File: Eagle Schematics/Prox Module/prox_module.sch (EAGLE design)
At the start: 52 parts, among them IC1 74LS14N, IC2 74LS14N, Q1 16MHZ

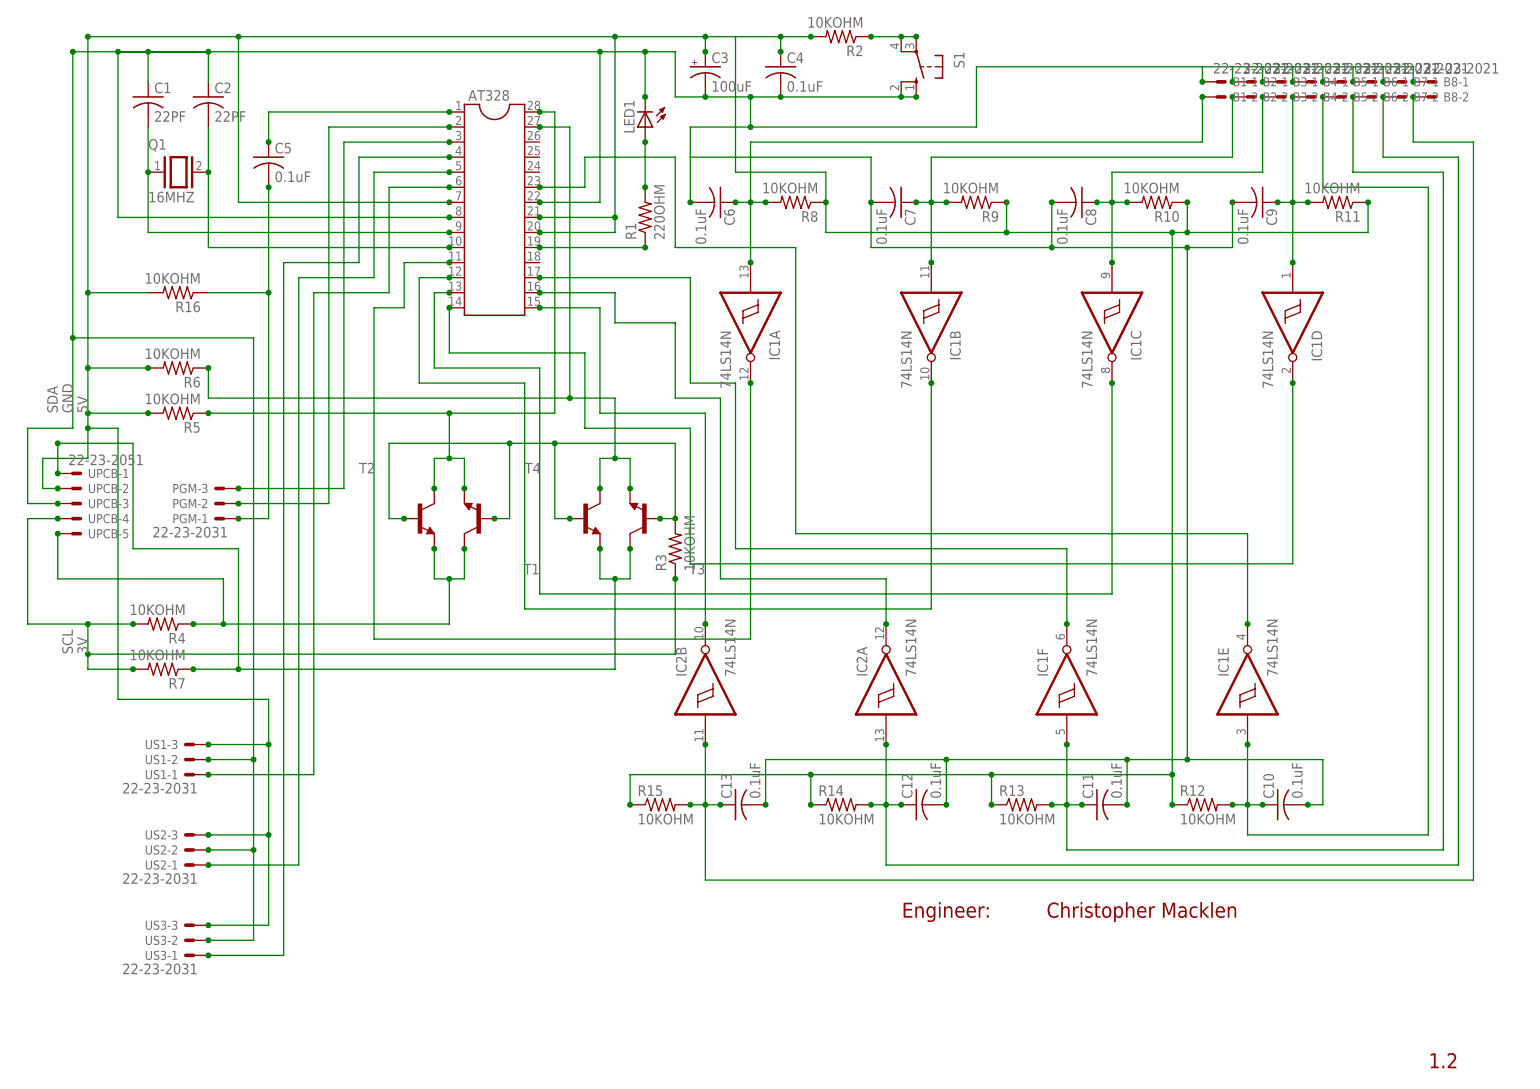
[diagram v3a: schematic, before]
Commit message: Modified prox design, added BOM
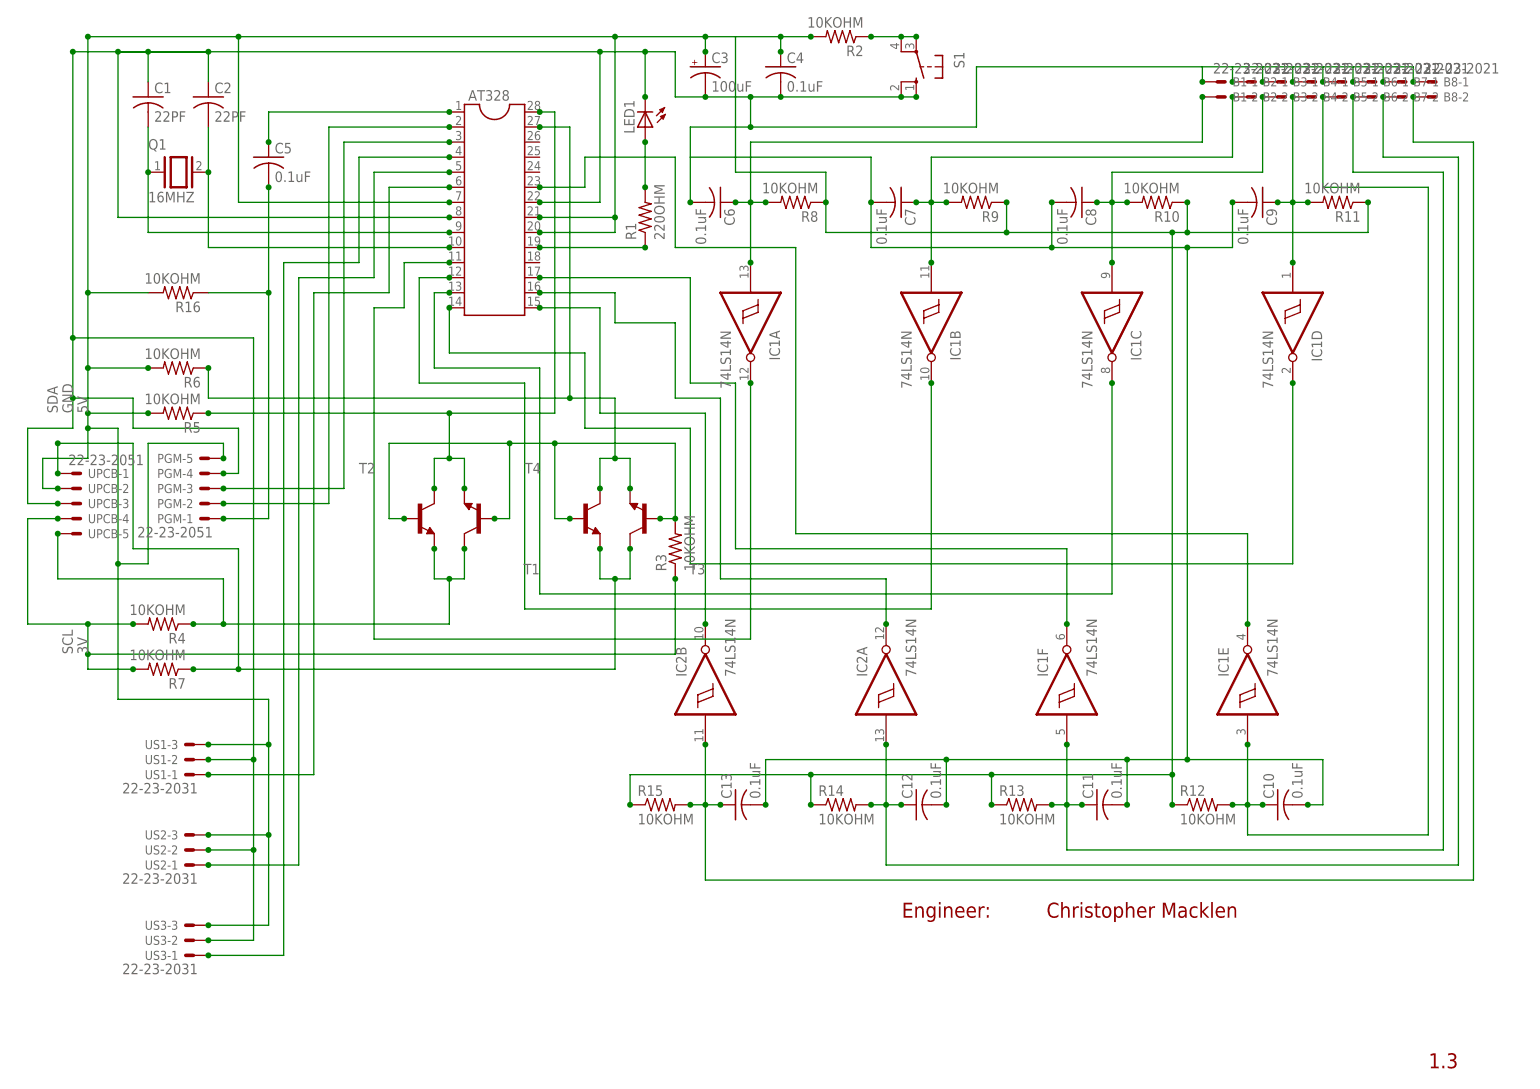
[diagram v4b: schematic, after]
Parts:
- PGM: value 22-23-2031 -> 22-23-2051; device con-molex:22-23-2031 -> con-molex:22-23-2051
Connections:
- net 5V: now also PGM-5.S
- net GND: now also PGM-4.S
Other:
- note added: "1.3"
- note removed: "1.2"
- moved on the sheet: PGM-1, PGM-2, PGM-3
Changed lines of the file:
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@@
 <part name="B7" library="con-molex" deviceset="22-23-2021" device=""/>
 <part name="B8" library="con-molex" deviceset="22-23-2021" device=""/>
-<part name="PGM" library="con-molex" deviceset="22-23-2031" device=""/>
 <part name="US1" library="con-molex" deviceset="22-23-2031" device=""/>
 <part name="US2" library="con-molex" deviceset="22-23-2031" device=""/>
@@
 <part name="R16" library="rcl" deviceset="R-US_" device="0204/7" value="10KOHM"/>
 <part name="C3" library="rcl" deviceset="CPOL-US" device="E2-5" value="100uF"/>
+<part name="PGM" library="con-molex" deviceset="22-23-2051" device=""/>
 </parts>
 <sheets>
@@
 <plain>
 <text x="190.5" y="33.02" size="2.54" layer="94" font="vector" align="center">Christopher Macklen</text>
-<text x="241.3" y="7.62" size="2.54" layer="94" font="vector" align="center">1.2</text>
+<text x="241.3" y="7.62" size="2.54" layer="94" font="vector" align="center">1.3</text>
 <text x="157.48" y="33.02" size="2.54" layer="94" font="vector" align="center">Engineer:</text>
 </plain>
@@
 <instance part="B8" gate="-1" x="238.76" y="172.72"/>
 <instance part="B8" gate="-2" x="238.76" y="170.18"/>
-<instance part="PGM" gate="-1" x="35.56" y="99.06" rot="R180"/>
-<instance part="PGM" gate="-2" x="35.56" y="101.6" rot="R180"/>
-<instance part="PGM" gate="-3" x="35.56" y="104.14" rot="R180"/>
 <instance part="US1" gate="-1" x="30.48" y="55.88" rot="R180"/>
 <instance part="US1" gate="-2" x="30.48" y="58.42" rot="R180"/>
@@
 <instance part="R16" gate="G$1" x="27.94" y="137.16" rot="R180"/>
 <instance part="C3" gate="G$1" x="116.84" y="175.26"/>
+<instance part="PGM" gate="-1" x="33.02" y="99.06" rot="R180"/>
+<instance part="PGM" gate="-2" x="33.02" y="101.6" rot="R180"/>
+<instance part="PGM" gate="-3" x="33.02" y="104.14" rot="R180"/>
+<instance part="PGM" gate="-4" x="33.02" y="106.68" rot="R180"/>
+<instance part="PGM" gate="-5" x="33.02" y="109.22" rot="R180"/>
 </instances>
 <busses>
@@
 <label x="10.16" y="116.84" size="1.778" layer="95" rot="R90"/>
 <pinref part="AT328" gate="G$1" pin="22"/>
-<wire x1="10.16" y1="114.3" x2="10.16" y2="129.54" width="0.1524" layer="91"/>
+<wire x1="10.16" y1="114.3" x2="10.16" y2="119.38" width="0.1524" layer="91"/>
+<wire x1="10.16" y1="119.38" x2="10.16" y2="129.54" width="0.1524" layer="91"/>
 <wire x1="10.16" y1="129.54" x2="10.16" y2="177.8" width="0.1524" layer="91"/>
 <wire x1="88.9" y1="152.4" x2="99.06" y2="152.4" width="0.1524" layer="91"/>
@@
 <pinref part="C3" gate="G$1" pin="-"/>
 <junction x="116.84" y="170.18"/>
+<pinref part="PGM" gate="-4" pin="S"/>
+<wire x1="35.56" y1="106.68" x2="38.1" y2="106.68" width="0.1524" layer="91"/>
+<wire x1="38.1" y1="106.68" x2="38.1" y2="114.3" width="0.1524" layer="91"/>
+<wire x1="38.1" y1="114.3" x2="20.32" y2="114.3" width="0.1524" layer="91"/>
+<wire x1="20.32" y1="114.3" x2="20.32" y2="119.38" width="0.1524" layer="91"/>
+<wire x1="20.32" y1="119.38" x2="10.16" y2="119.38" width="0.1524" layer="91"/>
+<junction x="10.16" y="119.38"/>
+<junction x="35.56" y="106.68"/>
 </segment>
 </net>
@@
 <net name="TX-RX" class="0">
 <segment>
-<wire x1="38.1" y1="101.6" x2="53.34" y2="101.6" width="0.1524" layer="91"/>
+<wire x1="35.56" y1="101.6" x2="53.34" y2="101.6" width="0.1524" layer="91"/>
 <wire x1="53.34" y1="101.6" x2="53.34" y2="165.1" width="0.1524" layer="91"/>
 <pinref part="AT328" gate="G$1" pin="2"/>
@@
 <junction x="73.66" y="165.1"/>
 <pinref part="PGM" gate="-2" pin="S"/>
-<junction x="38.1" y="101.6"/>
+<junction x="35.56" y="101.6"/>
 </segment>
 </net>
 <net name="RX-TX" class="0">
 <segment>
-<wire x1="38.1" y1="104.14" x2="55.88" y2="104.14" width="0.1524" layer="91"/>
+<wire x1="35.56" y1="104.14" x2="55.88" y2="104.14" width="0.1524" layer="91"/>
 <wire x1="55.88" y1="104.14" x2="55.88" y2="162.56" width="0.1524" layer="91"/>
 <pinref part="AT328" gate="G$1" pin="3"/>
@@
 <junction x="73.66" y="162.56"/>
 <pinref part="PGM" gate="-3" pin="S"/>
-<junction x="38.1" y="104.14"/>
+<junction x="35.56" y="104.14"/>
 </segment>
 </net>
@@
 <wire x1="43.18" y1="99.06" x2="43.18" y2="137.16" width="0.1524" layer="91"/>
 <wire x1="43.18" y1="137.16" x2="43.18" y2="154.94" width="0.1524" layer="91"/>
-<wire x1="38.1" y1="99.06" x2="43.18" y2="99.06" width="0.1524" layer="91"/>
-<pinref part="PGM" gate="-1" pin="S"/>
-<junction x="38.1" y="99.06"/>
+<wire x1="35.56" y1="99.06" x2="43.18" y2="99.06" width="0.1524" layer="91"/>
 <pinref part="R16" gate="G$1" pin="1"/>
 <wire x1="33.02" y1="137.16" x2="43.18" y2="137.16" width="0.1524" layer="91"/>
 <junction x="43.18" y="137.16"/>
+<pinref part="PGM" gate="-1" pin="S"/>
+<junction x="35.56" y="99.06"/>
 </segment>
 </net>
@@
 <junction x="22.86" y="124.46"/>
 <wire x1="12.7" y1="114.3" x2="17.78" y2="114.3" width="0.1524" layer="91"/>
-<wire x1="17.78" y1="114.3" x2="17.78" y2="68.58" width="0.1524" layer="91"/>
+<wire x1="17.78" y1="114.3" x2="17.78" y2="91.44" width="0.1524" layer="91"/>
+<wire x1="17.78" y1="91.44" x2="17.78" y2="68.58" width="0.1524" layer="91"/>
 <wire x1="17.78" y1="68.58" x2="43.18" y2="68.58" width="0.1524" layer="91"/>
 <wire x1="43.18" y1="68.58" x2="43.18" y2="60.96" width="0.1524" layer="91"/>
@@
 <pinref part="C3" gate="G$1" pin="+"/>
 <junction x="116.84" y="177.8"/>
-</segment>
-</net>
+<pinref part="PGM" gate="-5" pin="S"/>
+<wire x1="35.56" y1="109.22" x2="35.56" y2="111.76" width="0.1524" layer="91"/>
+<wire x1="35.56" y1="111.76" x2="22.86" y2="111.76" width="0.1524" layer="91"/>
+<wire x1="22.86" y1="111.76" x2="22.86" y2="91.44" width="0.1524" layer="91"/>
+<wire x1="22.86" y1="91.44" x2="17.78" y2="91.44" width="0.1524" layer="91"/>
+<junction x="17.78" y="91.44"/>
+<junction x="35.56" y="109.22"/>
+</segment>
+</net>

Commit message: Made final V1.4 revisions
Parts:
- added C14: 100uF, rcl:CPOL-USE2-5
- added C15: 0.1uF, rcl:C-US025-024X044
- ATMEGA: value (none) -> 328
- T1, T2, T3, T4: value (none) -> BJT
- renumbered AT328 to ATMEGA
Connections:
- net 3V: now also C14.+, C15.1
- net 5V: now also IC1P.VCC, IC2P.VCC
- net GND: now also C14.-, C15.2, IC1P.GND, IC2P.GND
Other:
- note added: "1.4"
- note removed: "1.3"
- moved on the sheet: R4, R7

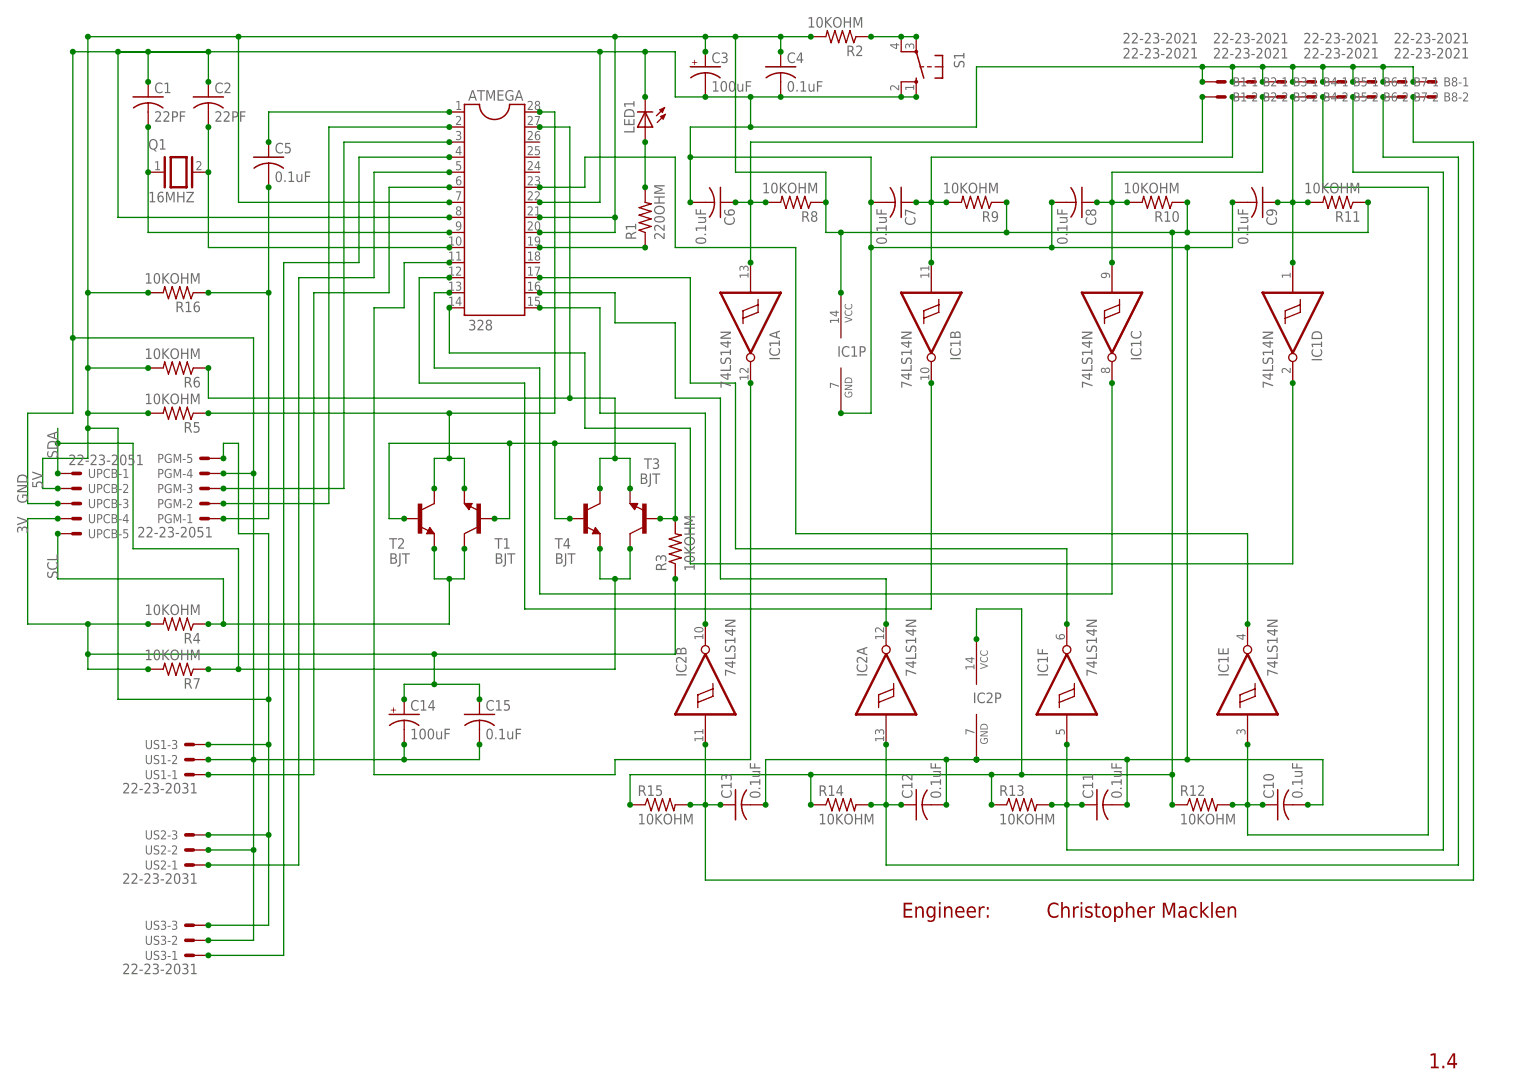
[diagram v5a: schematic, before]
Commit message: Modified all schematics
Added a self debugging system.
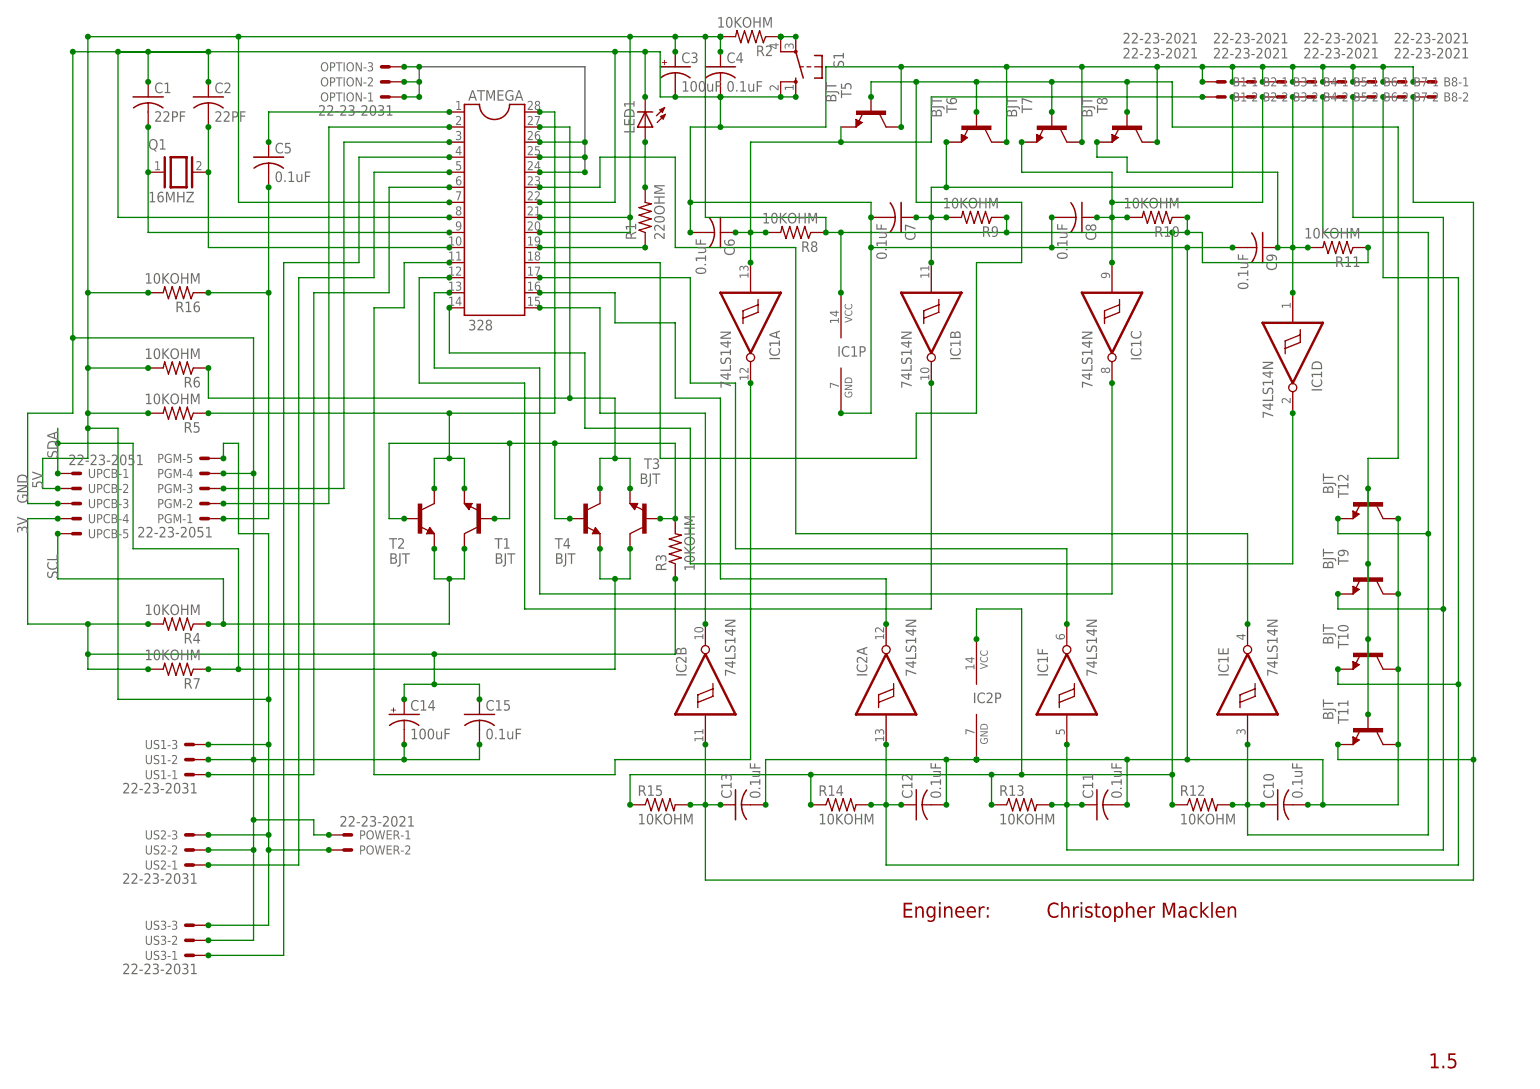
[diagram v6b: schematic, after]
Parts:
- added OPTION: 22-23-2031, con-molex:22-23-2031
- added POWER: 22-23-2021, con-molex:22-23-2021
- added T10, T11, T12, T5, T6, T7, T8, T9: BJT, transistor:-NPN-TO92-E1
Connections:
- removed net BMP-DBNCE1: B1-2.S, C6.1, IC1A.I, R8.2
- removed net BMP-DBNCE2: B2-2.S, C7.1, IC1B.I, R9.2
- removed net BMP-DBNCE3: B3-2.S, C8.1, IC1C.I, R10.2
- removed net BMP-DBNCE4: B4-2.S, C9.1, IC1D.I, R11.2
- removed net BMP-DBNCE5: B5-2.S, C10.1, IC1E.I, R12.2
- removed net BMP-DBNCE6: B6-2.S, C11.1, IC1F.I, R13.2
- removed net BMP-DBNCE7: B7-2.S, C12.1, IC2A.I, R14.2
- removed net BMP-DBNCE8: B8-2.S, C13.1, IC2B.I, R15.2
- new net BMP-IN1: B1-2.S, C6.1, IC1A.I, R8.2, T5.E
- new net BMP-IN2: B2-2.S, C7.1, IC1B.I, R9.2, T6.E
- new net BMP-IN3: B3-2.S, C8.1, IC1C.I, R10.2, T7.E
- new net BMP-IN4: B4-2.S, C9.1, IC1D.I, R11.2, T8.E
- new net BMP-IN5: B5-2.S, C10.1, IC1E.I, R12.2, T12.E
- new net BMP-IN6: B6-2.S, C11.1, IC1F.I, R13.2, T9.E
- new net BMP-IN7: B7-2.S, C12.1, IC2A.I, R14.2, T10.E
- new net BMP-IN8: B8-2.S, C13.1, IC2B.I, R15.2, T11.E
- new net OPTION1: ATMEGA.24, OPTION-1.S
- new net OPTION2: ATMEGA.25, OPTION-2.S
- new net OPTION3: ATMEGA.26, OPTION-3.S
- new net TEST: ATMEGA.18, T10.B, T11.B, T12.B, T5.B, T6.B, T7.B, T8.B, T9.B
- net 5V: now also POWER-2.S
- net GND: now also POWER-1.S, T10.C, T11.C, T12.C, T5.C, T6.C, T7.C, T8.C, T9.C
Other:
- note added: "1.5"
- note removed: "1.4"
- moved on the sheet: C3, C4, C6, C7, C8, C9, IC1D, R10, R11, R2, R8, R9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
